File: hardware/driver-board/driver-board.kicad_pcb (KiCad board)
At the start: 2 copper layers, 31 parts, among them J1 Conn_01x10_Male, U1 TXS0108E, U2 ME6210, U3 ME6210, U4 TLV61046ADB, U5 NC7SZ125, U6 FT813, U7 ER-TFT040-2, X1 YSX321SL

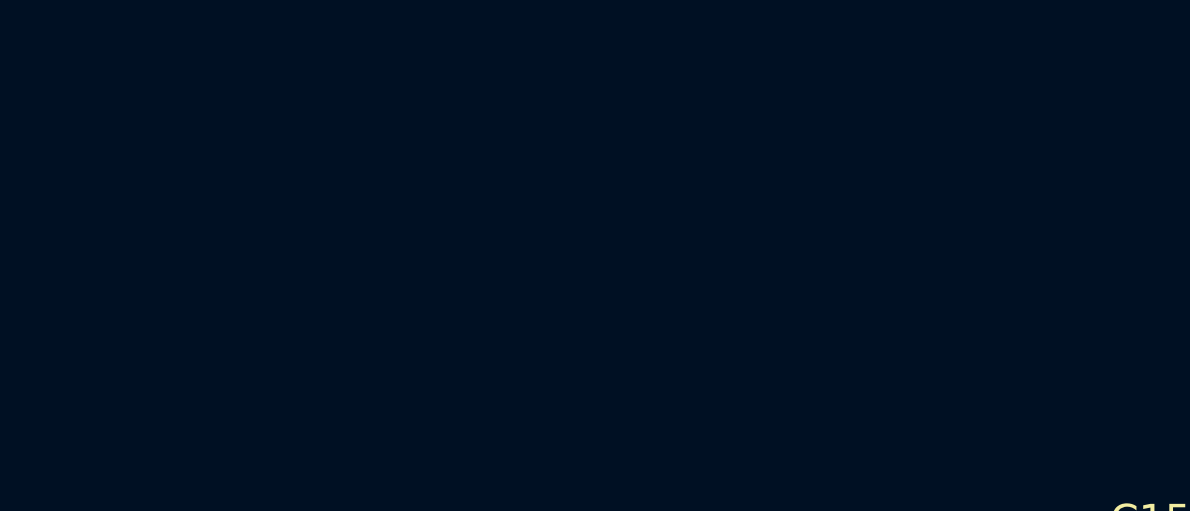
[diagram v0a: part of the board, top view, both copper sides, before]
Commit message: Add testpoints
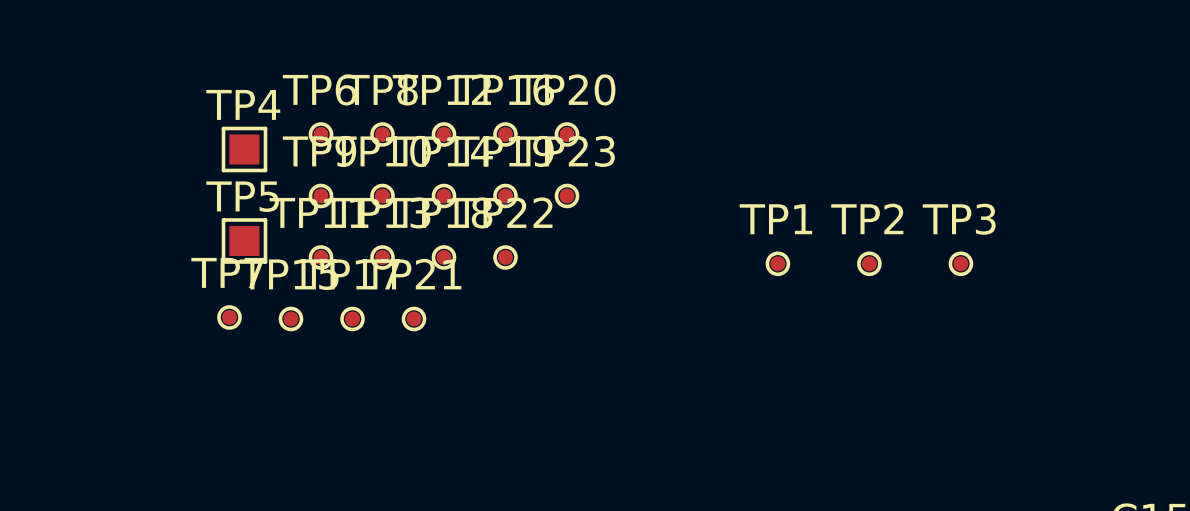
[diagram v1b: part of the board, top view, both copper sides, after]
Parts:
- added TP1: TestPoint, TestPoint:TestPoint_Pad_D0.5mm, F.Cu at (154.7, 55.6)
- added TP10: TestPoint, TestPoint:TestPoint_Pad_D0.5mm, F.Cu at (141.5, 53.4)
- added TP11: TestPoint, TestPoint:TestPoint_Pad_D0.5mm, F.Cu at (139.5, 55.4)
- added TP12: TestPoint, TestPoint:TestPoint_Pad_D0.5mm, F.Cu at (143.6, 51.3)
- added TP13: TestPoint, TestPoint:TestPoint_Pad_D0.5mm, F.Cu at (141.5, 55.4)
- added TP14: TestPoint, TestPoint:TestPoint_Pad_D0.5mm, F.Cu at (143.6, 53.4)
- added TP15: TestPoint, TestPoint:TestPoint_Pad_D0.5mm, F.Cu at (138.5, 57.5)
- added TP16: TestPoint, TestPoint:TestPoint_Pad_D0.5mm, F.Cu at (145.6, 51.3)
- added TP17: TestPoint, TestPoint:TestPoint_Pad_D0.5mm, F.Cu at (140.5, 57.5)
- added TP18: TestPoint, TestPoint:TestPoint_Pad_D0.5mm, F.Cu at (143.6, 55.4)
- added TP19: TestPoint, TestPoint:TestPoint_Pad_D0.5mm, F.Cu at (145.6, 53.4)
- added TP2: TestPoint, TestPoint:TestPoint_Pad_D0.5mm, F.Cu at (157.7, 55.6)
- added TP20: TestPoint, TestPoint:TestPoint_Pad_D0.5mm, F.Cu at (147.7, 51.3)
- added TP21: TestPoint, TestPoint:TestPoint_Pad_D0.5mm, F.Cu at (142.6, 57.5)
- added TP22: TestPoint, TestPoint:TestPoint_Pad_D0.5mm, F.Cu at (145.6, 55.4)
- added TP23: TestPoint, TestPoint:TestPoint_Pad_D0.5mm, F.Cu at (147.7, 53.4)
- added TP3: TestPoint, TestPoint:TestPoint_Pad_D0.5mm, F.Cu at (160.8, 55.6)
- added TP4: TestPoint, TestPoint:TestPoint_Pad_1.0x1.0mm, F.Cu at (136.9, 51.8)
- added TP5: TestPoint, TestPoint:TestPoint_Pad_1.0x1.0mm, F.Cu at (136.9, 54.9)
- added TP6: TestPoint, TestPoint:TestPoint_Pad_D0.5mm, F.Cu at (139.5, 51.3)
- added TP7: TestPoint, TestPoint:TestPoint_Pad_D0.5mm, F.Cu at (136.4, 57.4)
- added TP8: TestPoint, TestPoint:TestPoint_Pad_D0.5mm, F.Cu at (141.5, 51.3)
- added TP9: TestPoint, TestPoint:TestPoint_Pad_D0.5mm, F.Cu at (139.5, 53.4)

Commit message: PCB layout on work
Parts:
- removed TP1: TestPoint, TestPoint:TestPoint_Pad_D0.5mm
- added 12V: TestPoint, TestPoint:TestPoint_Pad_D0.5mm, F.Cu at (139.5, 50.3)
- moved C5 62.4 mm to (118.5, 57.5), turned to 180 degrees
- moved C6 62.4 mm to (118.5, 62.5), turned to 180 degrees
- moved R1 57.1 mm to (136.9, 50.3), turned to 180 degrees
- moved C7 56.8 mm to (132.9, 52.0), turned to 180 degrees
- moved U3 56.7 mm to (118.5, 60.0), turned to 90 degrees
- moved R2 55.6 mm to (133.6, 54.5), turned to 90 degrees
- moved L1 55.4 mm to (136.6, 55.7)
- moved C3 54.3 mm to (126.5, 57.5), turned to 180 degrees
- moved C4 54.0 mm to (126.5, 62.5), turned to 180 degrees
- moved C8 52.1 mm to (139.4, 52.8), turned to 270 degrees
- moved U2 51.7 mm to (126.5, 60.0), turned to 90 degrees
- moved U7 46.4 mm to (148.0, 66.5)
- moved U4 44.0 mm to (136.5, 53.0), turned to 180 degrees
- moved U5 37.2 mm to (126.5, 68.5), turned to 180 degrees
- moved U1 32.9 mm to (120.5, 69.5), turned to 180 degrees
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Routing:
- net +12V: track 0.00 -> 17.1 mm
- net Net-(R1-Pad2): track 0.00 -> 3.57 mm
- net +5V: track 0.00 -> 3.56 mm
- net Net-(L1-Pad2): track 0.00 -> 1.84 mm
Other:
- copper layers 2 -> 4
- net class Default: trace_width 0.25 -> 0.2; via_dia 0.8 -> 0.45; via_drill 0.4 -> 0.2
- rule via_min_drill: 0.3 -> 0.2
- rule via_min_size: 0.4 -> 0.45

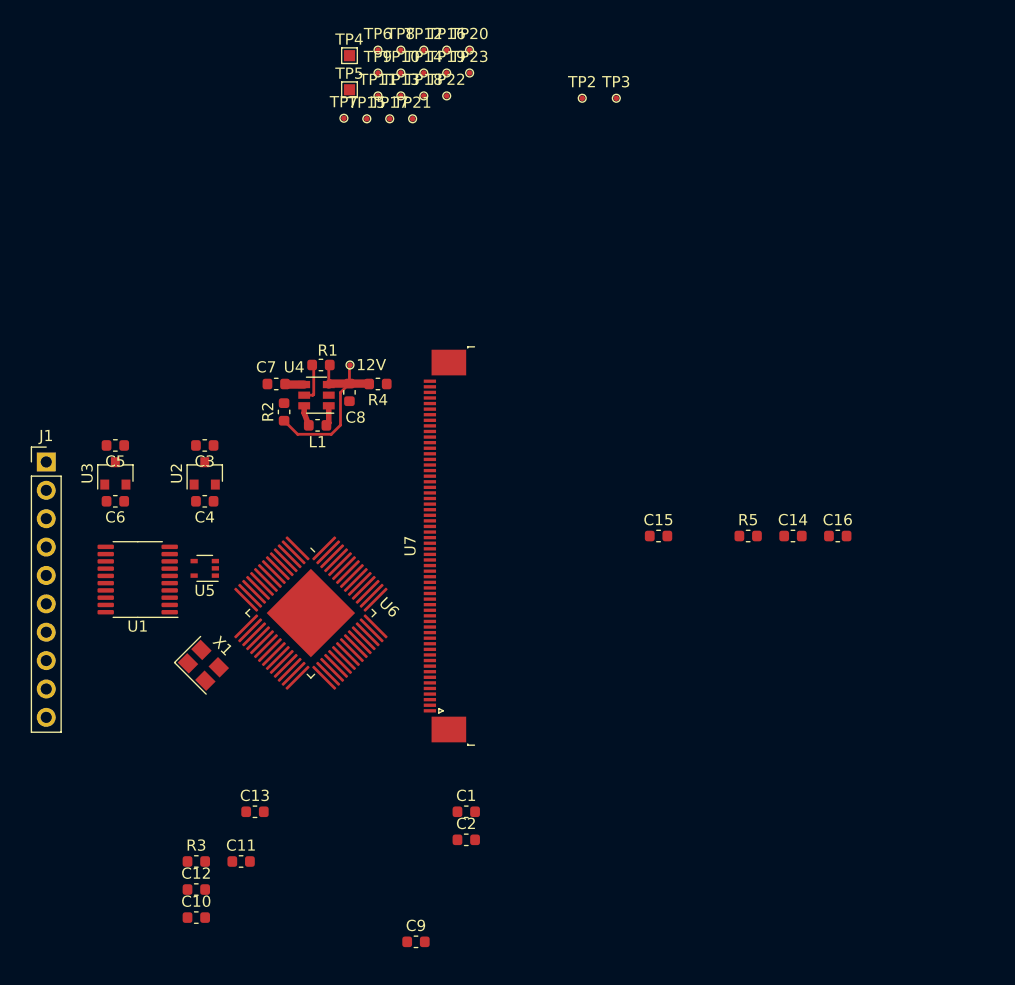
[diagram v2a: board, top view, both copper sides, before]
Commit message: Update display connector footprint to hand solder
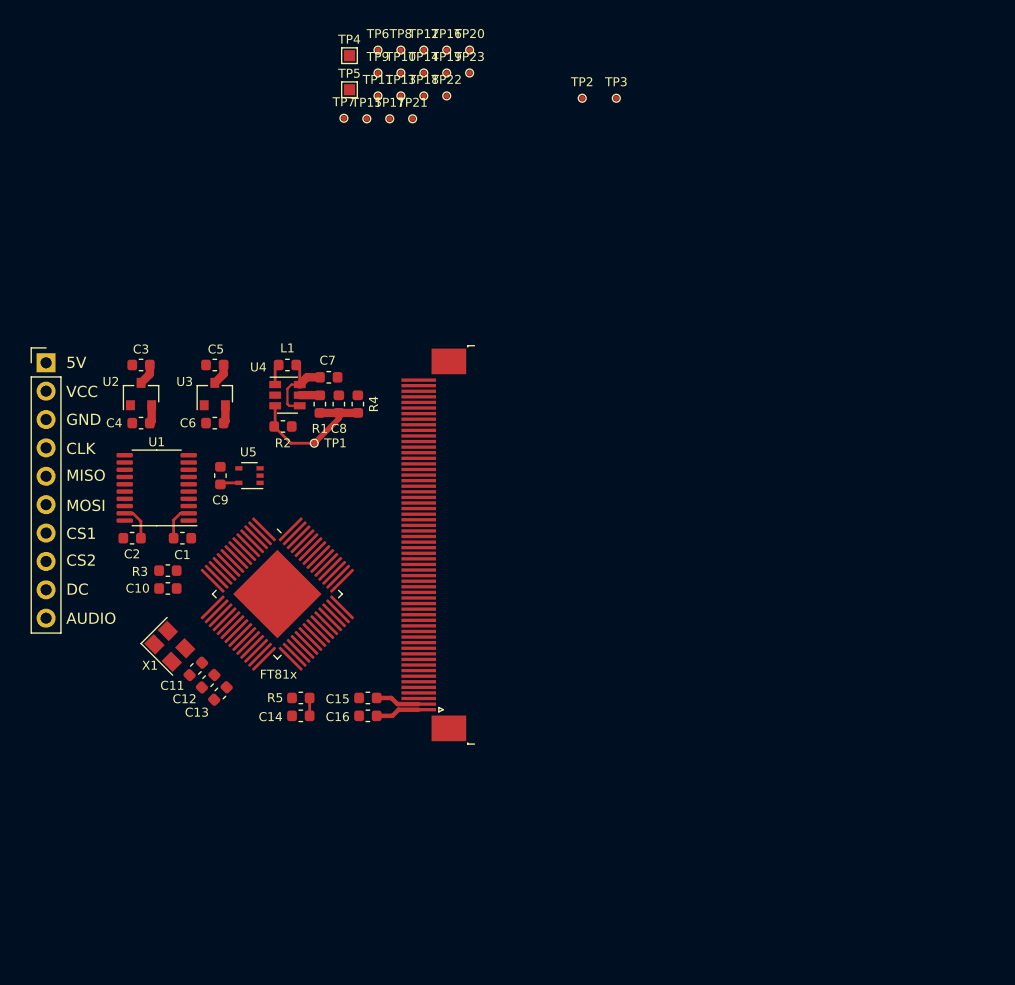
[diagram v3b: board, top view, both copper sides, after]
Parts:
- U7: footprint Connector_FFC-FPC:TE_5-1734839-0_1x60-1MP_P0.5mm_Horizontal -> Connector_FFC-FPC:TE_5-1734839-0_1x60-1MP_P0.5mm_Horizontal_HandSolder
- moved C14 46.9 mm to (135.1, 81.7)
- moved C9 45.2 mm to (127.9, 60.2), turned to 90 degrees
- moved C16 45.0 mm to (141.1, 81.7), turned to 180 degrees
- moved R5 42.6 mm to (135.1, 80.1), turned to 180 degrees
- moved C2 40.3 mm to (120.0, 65.8), turned to 180 degrees
- moved C1 35.3 mm to (124.5, 65.8)
- moved C15 29.8 mm to (141.1, 80.1), turned to 180 degrees
- moved C10 29.6 mm to (123.2, 70.3), turned to 180 degrees
- moved R3 26.2 mm to (123.2, 68.7), turned to 180 degrees
- moved C12 18.7 mm to (126.8, 78.6), turned to 225 degrees
- moved C11 17.7 mm to (125.7, 77.5), turned to 225 degrees
- moved C5 11.4 mm to (127.4, 50.3)
- moved U3 11.4 mm to (127.4, 52.9)
- moved C6 11.3 mm to (127.4, 55.5)
- moved C13 11.0 mm to (127.9, 79.7), turned to 225 degrees
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- renumbered U6 to FT81x, 12V to TP1
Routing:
- net +3V0: track 0.00 -> 14.6 mm
- net +5V: track 3.56 -> 11.6 mm
- net +12V: track 17.1 -> 13.1 mm
- net VCC: track 0.00 -> 3.26 mm
- net Net-(R1-Pad2): track 3.57 -> 1.81 mm
- net +3V3: track 0.00 -> 1.67 mm
- net DISPRES: track 0.00 -> 1.60 mm
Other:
- board text added: "5V"
- board text added: "AUDIO"
- board text added: "CLK"
- board text added: "CS1"
- board text added: "CS2"
- board text added: "DC"
- board text added: "GND"
- board text added: "MISO"
- board text added: "MOSI"
- board text added: "VCC"

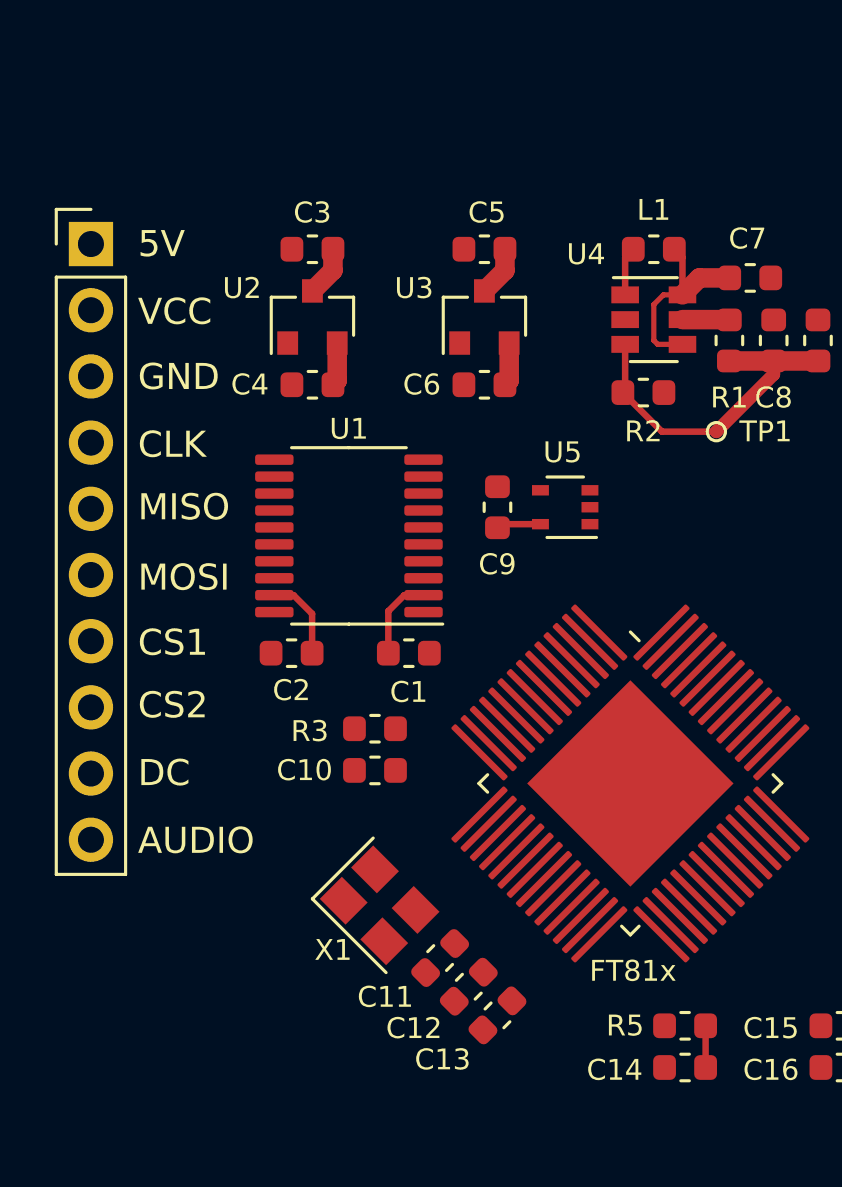
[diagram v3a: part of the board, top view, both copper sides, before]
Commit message: Add more pin header pins
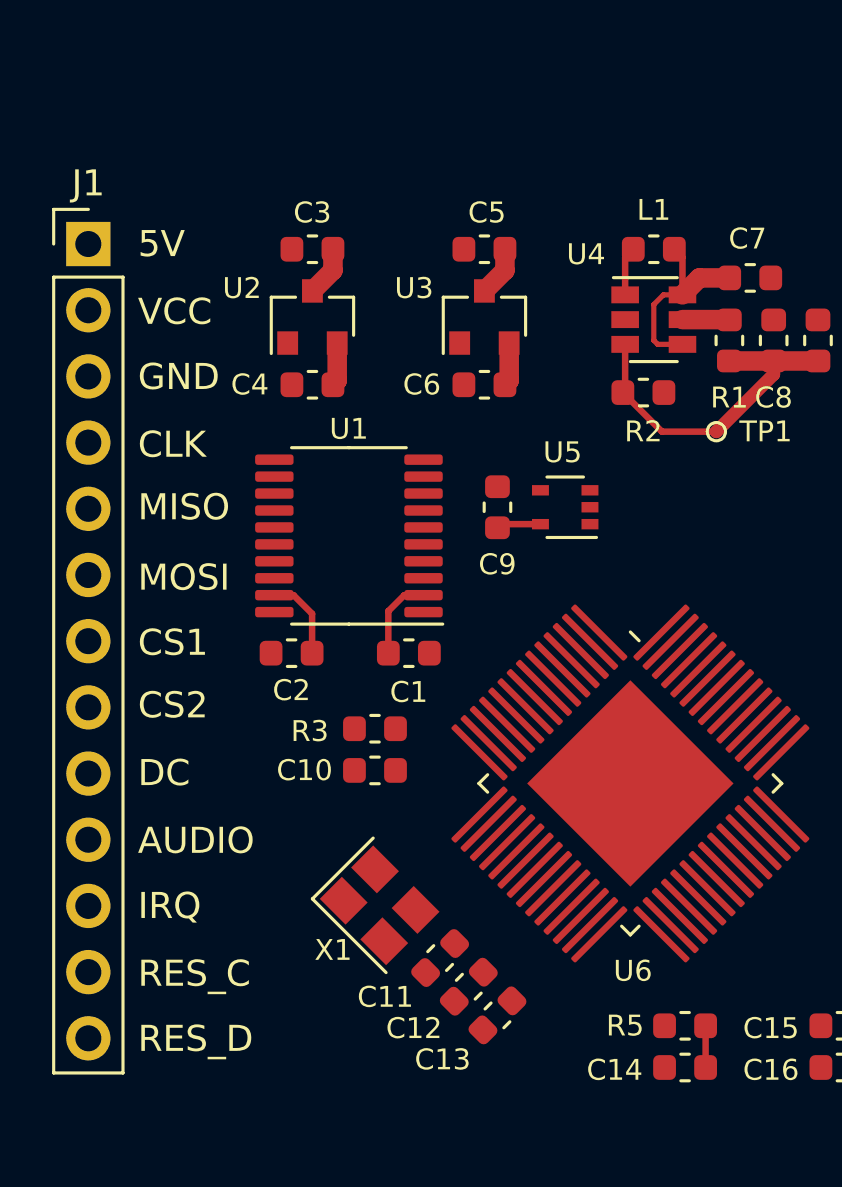
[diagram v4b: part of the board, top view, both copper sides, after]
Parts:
- J1: value Conn_01x10_Male -> Conn_01x13_Male; footprint Connector_PinHeader_2.54mm:PinHeader_1x10_P2.54mm_Vertical -> Connector_PinHeader_2.54mm:PinHeader_1x13_P2.54mm_Vertical
- moved J1 0.10 mm to (112.2, 50.1)
- renumbered FT81x to U6
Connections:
- C10 pad 1: Net-(C10-Pad1) -> FTRES
- R3 pad 1: Net-(C10-Pad1) -> FTRES
- U6 pad 14: Net-(C10-Pad1) -> FTRES
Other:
- board text added: "IRQ"
- board text added: "RES_C"
- board text added: "RES_D"

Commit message: Board layout on work
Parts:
- added TP24: TestPoint, TestPoint:TestPoint_Pad_D0.5mm, F.Cu at (114.6, 80.1)
- added TP25: TestPoint, TestPoint:TestPoint_Pad_D0.5mm, F.Cu at (114.6, 77.4)
- moved TP19 67.4 mm to (114.6, 82.6)
- moved TP11 61.0 mm to (133.6, 86.6)
- moved TP13 60.9 mm to (135.8, 86.6)
- moved TP4 60.6 mm to (120.5, 80.2)
- moved TP12 59.3 mm to (114.6, 72.4)
- moved TP21 55.7 mm to (114.6, 74.9)
- moved TP10 54.3 mm to (114.6, 69.8)
- moved TP16 54.3 mm to (114.6, 64.8)
- moved TP8 53.9 mm to (114.6, 67.3)
- moved TP3 52.4 mm to (120.8, 57.0)
- moved TP15 50.4 mm to (140.0, 78.7)
- moved TP17 50.0 mm to (141.7, 78.2)
- moved TP7 49.5 mm to (139.5, 77.7)
- moved TP14 49.4 mm to (114.6, 62.2)
- moved TP6 46.5 mm to (114.6, 59.7)
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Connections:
- U6 pad 13: Net-(U6-Pad13) -> IRQ
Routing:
- net GND: track 0.00 -> 107.2 mm, vias 0 -> 34
- net MISO_3V: track 0.00 -> 53.6 mm, vias 0 -> 2
- net CLK_3V: track 0.00 -> 52.1 mm, vias 0 -> 2
- net MOSI_3V: track 0.00 -> 51.0 mm, vias 0 -> 2
- net DISPRES: track 1.60 -> 39.4 mm
- net +3V3: track 1.67 -> 37.0 mm, vias 0 -> 2
- net VSYNC: track 0.00 -> 30.9 mm, vias 0 -> 2
- net +3V0: track 14.6 -> 45.0 mm, vias 0 -> 12
- net HSYNC: track 0.00 -> 29.4 mm, vias 0 -> 2
- net DE: track 0.00 -> 28.6 mm, vias 0 -> 2
- net PCLK: track 0.00 -> 27.6 mm, vias 0 -> 2
- net AUDIO: track 0.00 -> 25.8 mm, vias 0 -> 2
- net FTRES: track 0.00 -> 22.8 mm, vias 0 -> 2
- net IRQ: track 0.00 -> 20.0 mm, vias 0 -> 2
- net B0: track 0.00 -> 18.5 mm
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- added copper zone on In2.Cu, net +3V0
- added copper zone on In2.Cu, net +5V
- added copper zone on In1.Cu, net GND
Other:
- board outline added: 42.2 x 36.8 mm
- net class Default: trace_width 0.2 -> 0.25
- rule trace_min: 0.2 -> 0.25
- board text added: "12V"
- board text added: "3.3V"
- board text added: "3V"
- board text added: "DE"
- board text added: "HS"
- board text added: "PC"
- board text added: "VS"
